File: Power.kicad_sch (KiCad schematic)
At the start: 0 parts

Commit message: Add screw terminal power input and symbol
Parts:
- added C17: 10uF, symbol Device:C
- added C18: 1uF, symbol Device:C
- added C19: 100nF, symbol Device:C
- added J3: 1986660-2, XuLab:CONN2_1986660-2_TEC, symbol XuLab:1986660-2
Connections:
- new net +7.4V: C17.1, C18.1, C19.1, J3.1A, J3.1B
- new net GND: C17.2, C18.2, C19.2, J3.2A, J3.2B

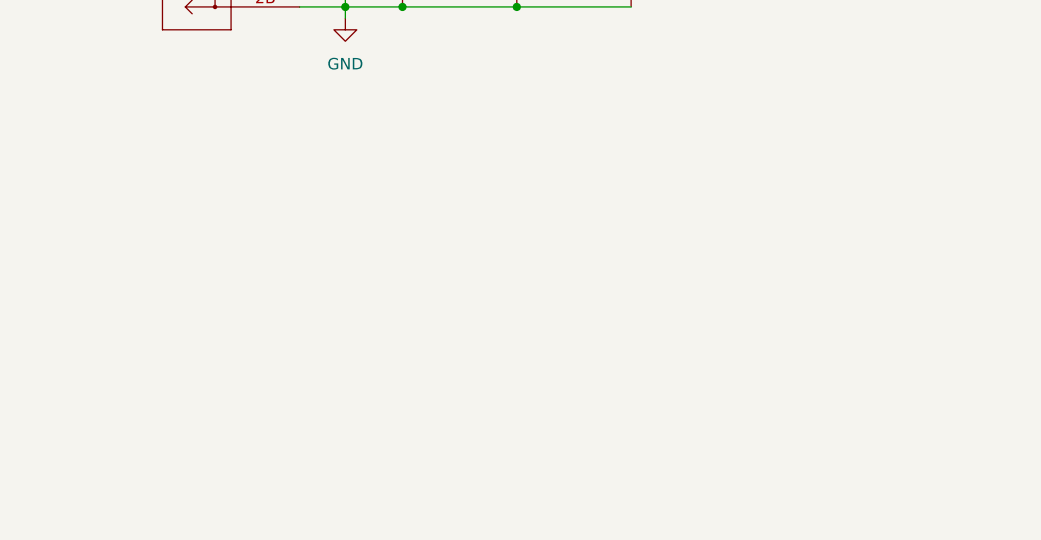
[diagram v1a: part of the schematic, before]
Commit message: Add 3v3 buck converter
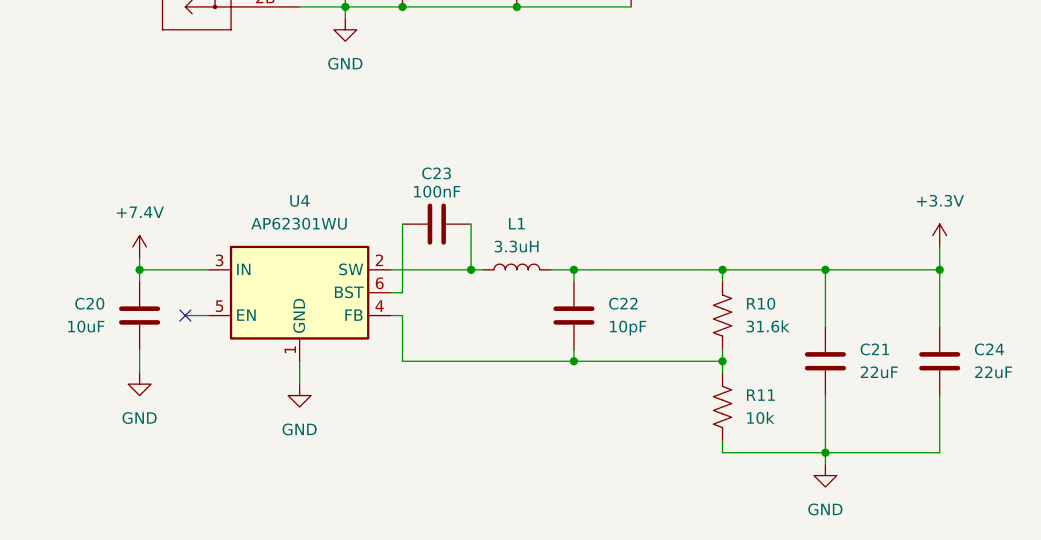
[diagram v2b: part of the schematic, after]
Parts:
- added C20: 10uF, symbol Device:C
- added C21, C24: 22uF, symbol Device:C
- added C22: 10pF, symbol Device:C
- added C23: 100nF, symbol Device:C
- added L1: 3.3uH, symbol Device:L
- added R10: 31.6k, symbol Device:R_US
- added R11: 10k, symbol Device:R_US
- added U4: AP62301WU, Package_TO_SOT_SMD:TSOT-23-6, symbol Regulator_Switching:AP62301WU
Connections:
- net +7.4V: now also C20.1, U4.3 (IN)
- net GND: now also C20.2, C21.2, C24.2, R11.2, U4.1 (GND)
- new net: C22.2, R10.2, R11.1, U4.4 (FB)
- new net: C23.2, L1.1, U4.2 (SW)
- new net: C23.1, U4.6 (BST)
- new net +3.3V: C21.1, C22.1, C24.1, L1.2, R10.1
- no-connect marks 0 -> 1

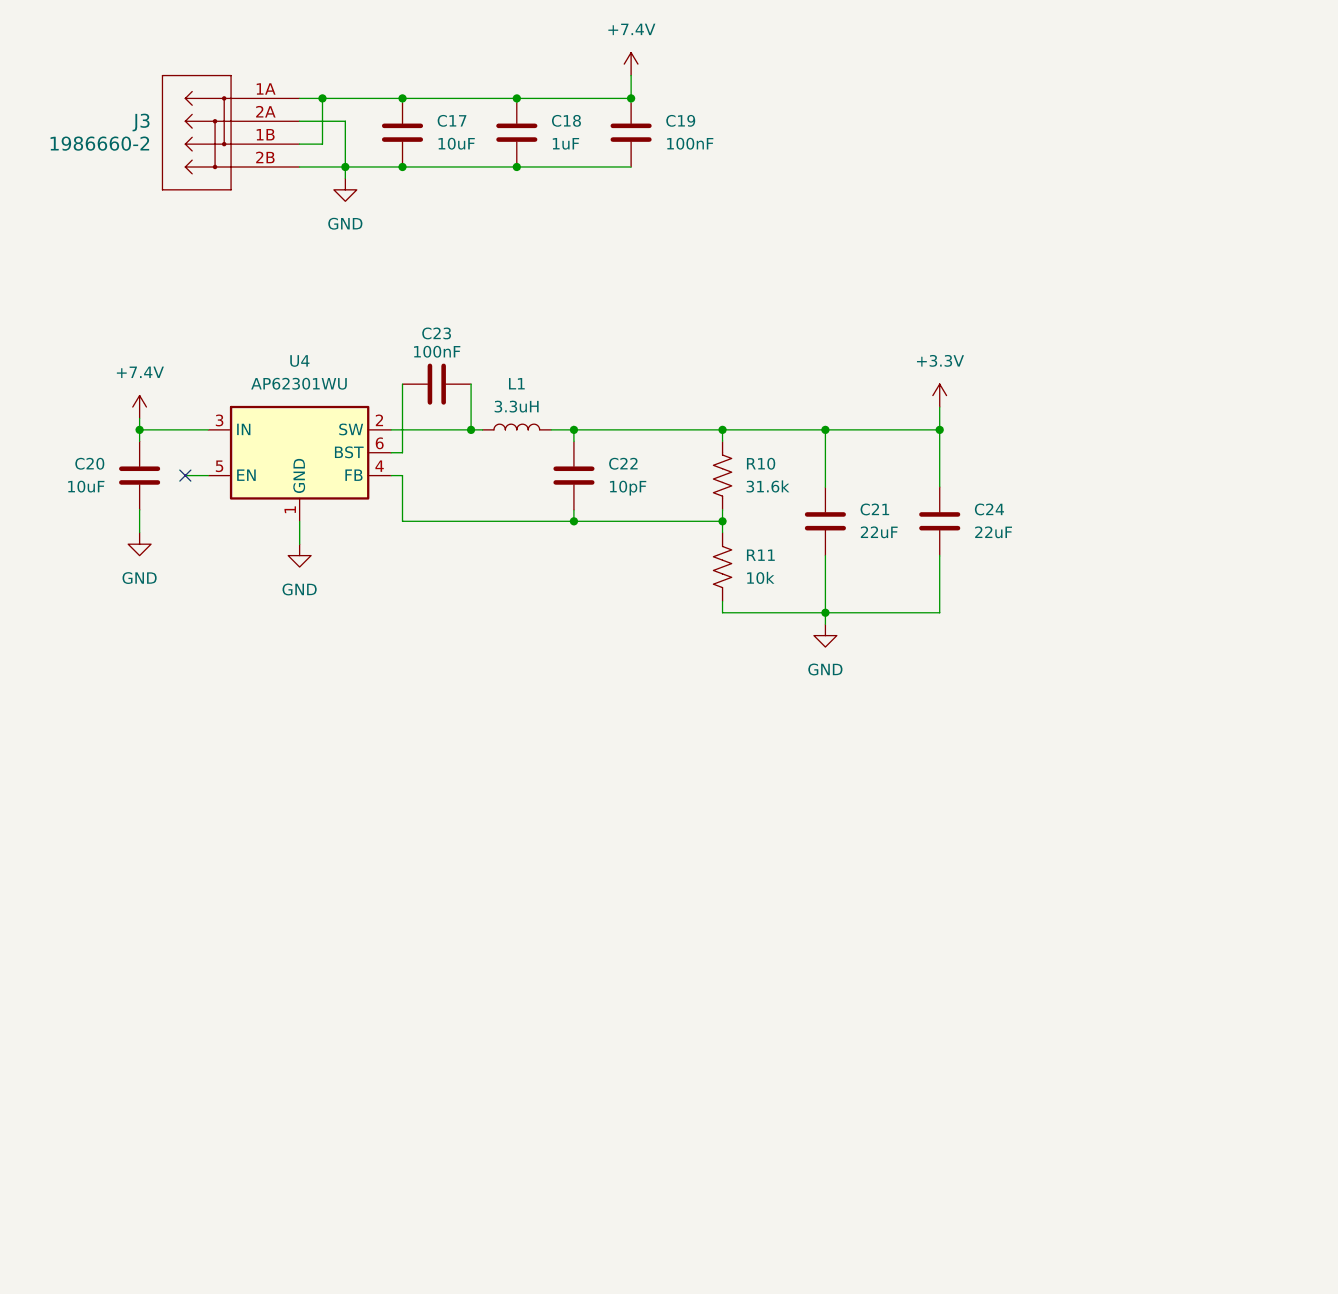
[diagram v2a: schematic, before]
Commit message: Add TVS diodes
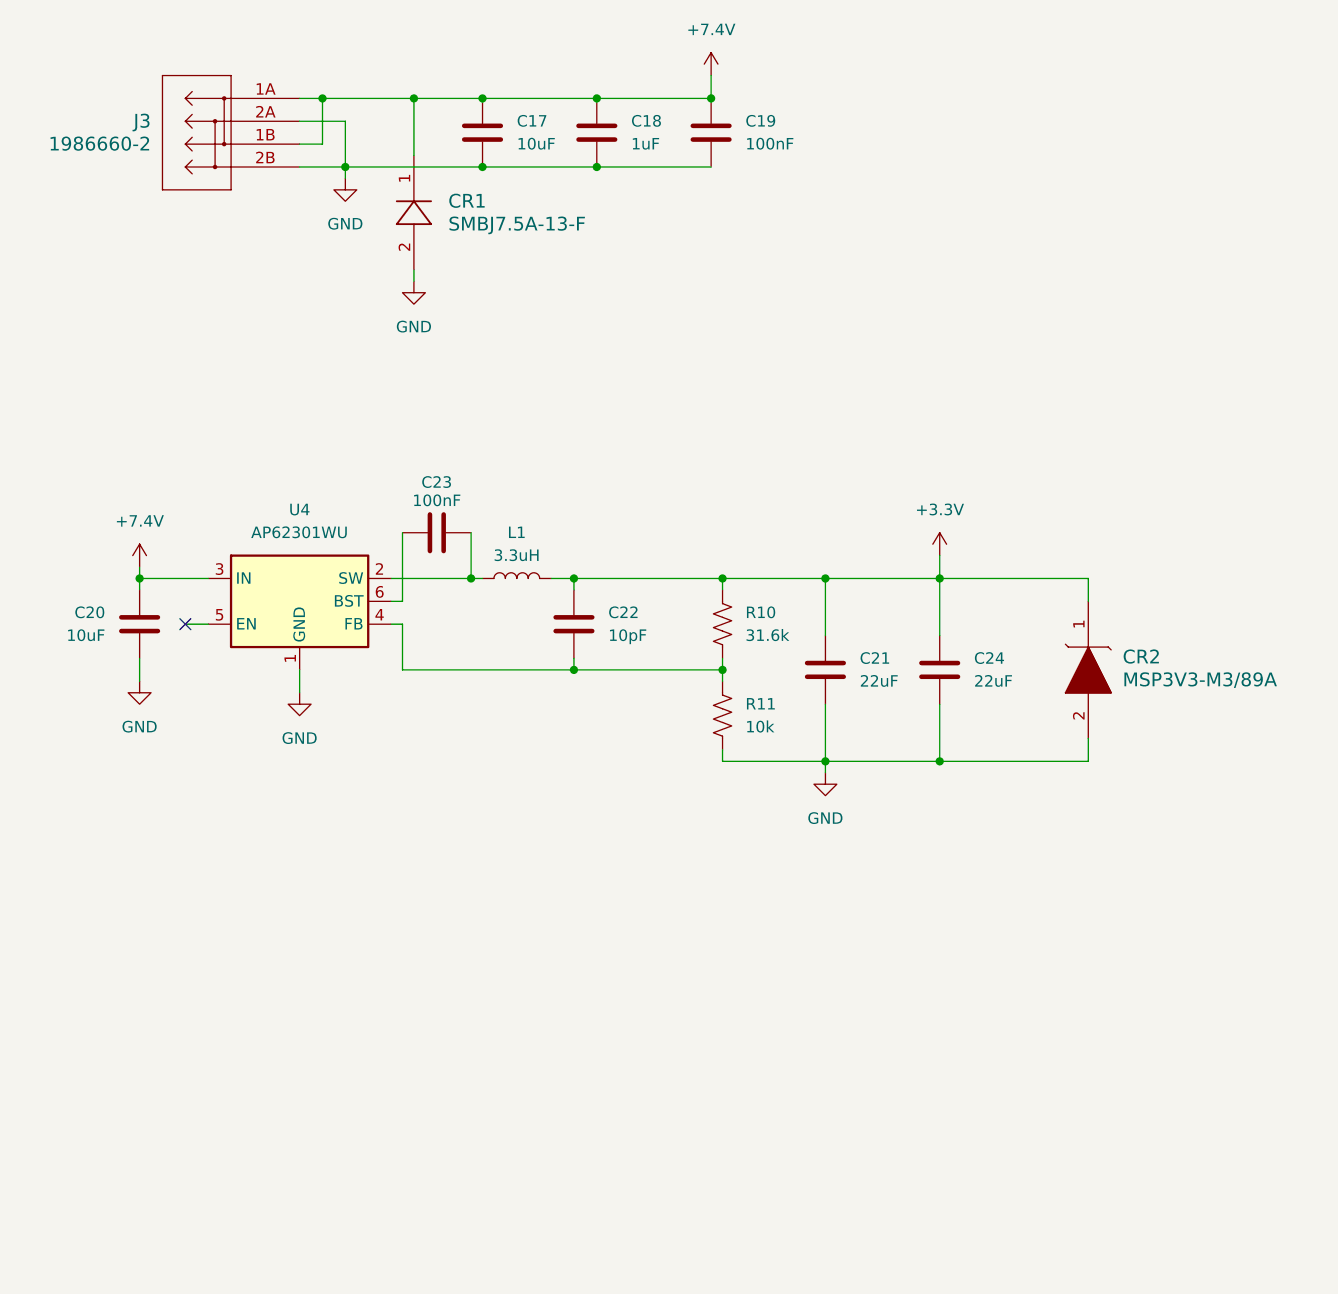
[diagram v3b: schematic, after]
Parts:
- added CR1: SMBJ7.5A-13-F, XuLab:SMB_DIO, symbol XuLab:SMBJ7.5A-13-F
- added CR2: MSP3V3-M3/89A, XuLab:DO-219AD_VIS, symbol XuLab:MSP3V3-M3_89A
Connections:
- net +3.3V: now also CR2.1
- net +7.4V: now also CR1.1
- net GND: now also CR1.2, CR2.2
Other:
- moved on the sheet: C17, C18, C19, C20, C21, C22, C23, C24, L1, R10, R11, U4

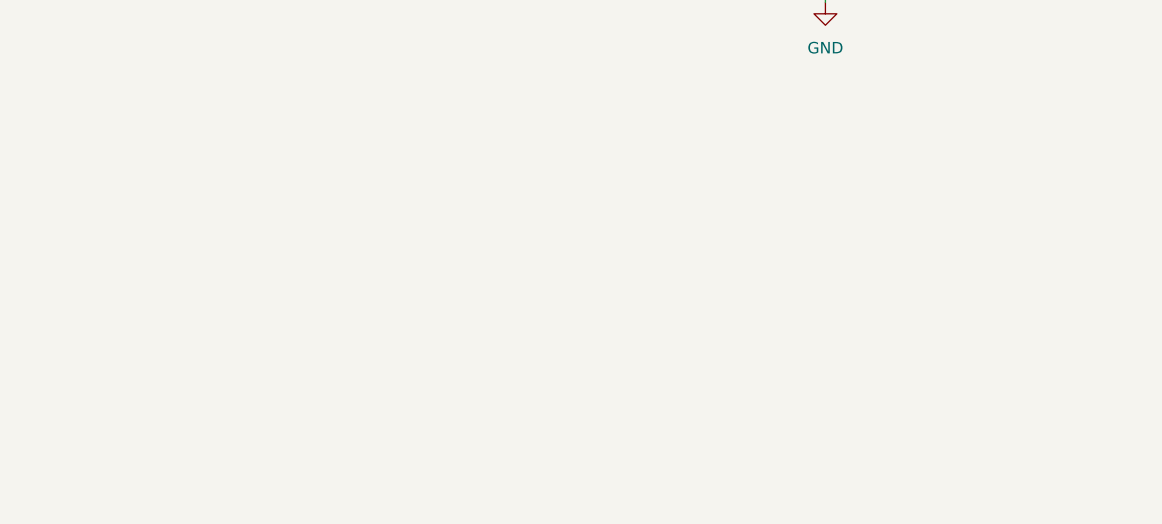
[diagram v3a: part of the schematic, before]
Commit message: Add connectors for servo power
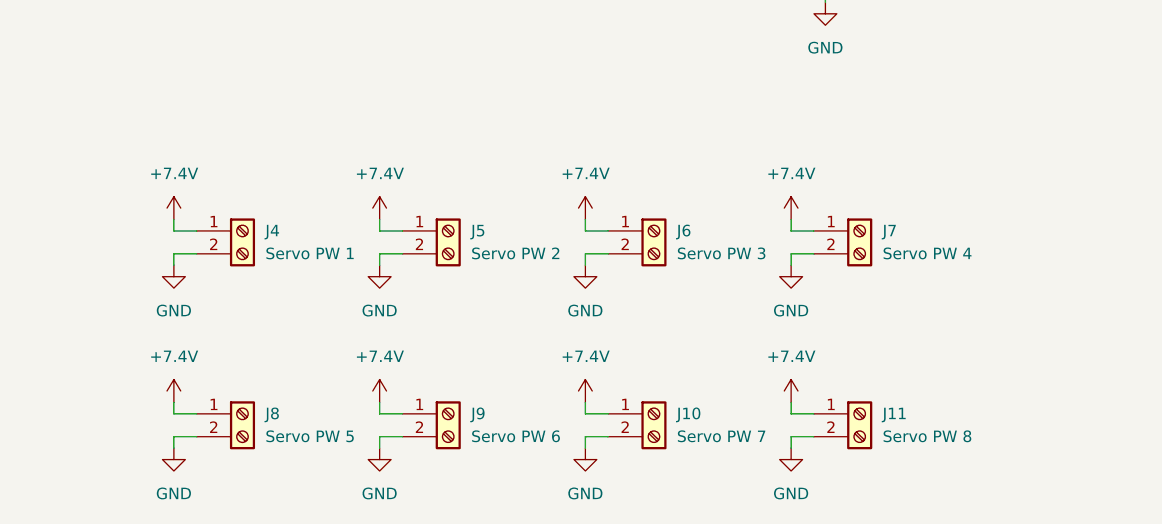
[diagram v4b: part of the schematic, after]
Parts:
- added J10: Servo PW 7, TerminalBlock_Phoenix:TerminalBlock_Phoenix_PT-1,5-2-5.0-H_1x02_P5.00mm_Horizontal, symbol Connector:Screw_Terminal_01x02
- added J11: Servo PW 8, TerminalBlock_Phoenix:TerminalBlock_Phoenix_PT-1,5-2-5.0-H_1x02_P5.00mm_Horizontal, symbol Connector:Screw_Terminal_01x02
- added J4: Servo PW 1, TerminalBlock_Phoenix:TerminalBlock_Phoenix_PT-1,5-2-5.0-H_1x02_P5.00mm_Horizontal, symbol Connector:Screw_Terminal_01x02
- added J5: Servo PW 2, TerminalBlock_Phoenix:TerminalBlock_Phoenix_PT-1,5-2-5.0-H_1x02_P5.00mm_Horizontal, symbol Connector:Screw_Terminal_01x02
- added J6: Servo PW 3, TerminalBlock_Phoenix:TerminalBlock_Phoenix_PT-1,5-2-5.0-H_1x02_P5.00mm_Horizontal, symbol Connector:Screw_Terminal_01x02
- added J7: Servo PW 4, TerminalBlock_Phoenix:TerminalBlock_Phoenix_PT-1,5-2-5.0-H_1x02_P5.00mm_Horizontal, symbol Connector:Screw_Terminal_01x02
- added J8: Servo PW 5, TerminalBlock_Phoenix:TerminalBlock_Phoenix_PT-1,5-2-5.0-H_1x02_P5.00mm_Horizontal, symbol Connector:Screw_Terminal_01x02
- added J9: Servo PW 6, TerminalBlock_Phoenix:TerminalBlock_Phoenix_PT-1,5-2-5.0-H_1x02_P5.00mm_Horizontal, symbol Connector:Screw_Terminal_01x02
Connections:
- net +7.4V: now also J10.1 (Pin_1), J11.1 (Pin_1), J4.1 (Pin_1), J5.1 (Pin_1), J6.1 (Pin_1), J7.1 (Pin_1), J8.1 (Pin_1), J9.1 (Pin_1)
- net GND: now also J10.2 (Pin_2), J11.2 (Pin_2), J4.2 (Pin_2), J5.2 (Pin_2), J6.2 (Pin_2), J7.2 (Pin_2), J8.2 (Pin_2), J9.2 (Pin_2)

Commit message: Add signal outputs for servos and change screw terminal footprints
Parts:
- J10, J11, J4, J5, J6, J7, J8, J9: footprint TerminalBlock_Phoenix:TerminalBlock_Phoenix_PT-1,5-2-5.0-H_1x02_P5.00mm_Horizontal -> TerminalBlock_Phoenix:TerminalBlock_Phoenix_MKDS-1,5-2_1x02_P5.00mm_Horizontal
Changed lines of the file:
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@@
 	(title_block
 		(title "Power")
-		(date "2025-10-24")
+		(date "2025-10-26")
 		(rev "A")
 		(company "CU Boulder Senior Design Team 29 - Xu Lab")
@@
 			)
 		)
-		(property "Footprint" "TerminalBlock_Phoenix:TerminalBlock_Phoenix_PT-1,5-2-5.0-H_1x02_P5.00mm_Horizontal"
+		(property "Footprint" "TerminalBlock_Phoenix:TerminalBlock_Phoenix_MKDS-1,5-2_1x02_P5.00mm_Horizontal"
 			(at 49.53 161.29 0)
 			(effects
@@
 			)
 		)
-		(property "Footprint" "TerminalBlock_Phoenix:TerminalBlock_Phoenix_PT-1,5-2-5.0-H_1x02_P5.00mm_Horizontal"
+		(property "Footprint" "TerminalBlock_Phoenix:TerminalBlock_Phoenix_MKDS-1,5-2_1x02_P5.00mm_Horizontal"
 			(at 118.11 140.97 0)
 			(effects
@@
 			)
 		)
-		(property "Footprint" "TerminalBlock_Phoenix:TerminalBlock_Phoenix_PT-1,5-2-5.0-H_1x02_P5.00mm_Horizontal"
+		(property "Footprint" "TerminalBlock_Phoenix:TerminalBlock_Phoenix_MKDS-1,5-2_1x02_P5.00mm_Horizontal"
 			(at 72.39 140.97 0)
 			(effects
@@
 			)
 		)
-		(property "Footprint" "TerminalBlock_Phoenix:TerminalBlock_Phoenix_PT-1,5-2-5.0-H_1x02_P5.00mm_Horizontal"
+		(property "Footprint" "TerminalBlock_Phoenix:TerminalBlock_Phoenix_MKDS-1,5-2_1x02_P5.00mm_Horizontal"
 			(at 95.25 140.97 0)
 			(effects
@@
 			)
 		)
-		(property "Footprint" "TerminalBlock_Phoenix:TerminalBlock_Phoenix_PT-1,5-2-5.0-H_1x02_P5.00mm_Horizontal"
+		(property "Footprint" "TerminalBlock_Phoenix:TerminalBlock_Phoenix_MKDS-1,5-2_1x02_P5.00mm_Horizontal"
 			(at 49.53 140.97 0)
 			(effects
@@
 			)
 		)
-		(property "Footprint" "TerminalBlock_Phoenix:TerminalBlock_Phoenix_PT-1,5-2-5.0-H_1x02_P5.00mm_Horizontal"
+		(property "Footprint" "TerminalBlock_Phoenix:TerminalBlock_Phoenix_MKDS-1,5-2_1x02_P5.00mm_Horizontal"
 			(at 72.39 161.29 0)
 			(effects
@@
 			)
 		)
-		(property "Footprint" "TerminalBlock_Phoenix:TerminalBlock_Phoenix_PT-1,5-2-5.0-H_1x02_P5.00mm_Horizontal"
+		(property "Footprint" "TerminalBlock_Phoenix:TerminalBlock_Phoenix_MKDS-1,5-2_1x02_P5.00mm_Horizontal"
 			(at 95.25 161.29 0)
 			(effects
@@
 			)
 		)
-		(property "Footprint" "TerminalBlock_Phoenix:TerminalBlock_Phoenix_PT-1,5-2-5.0-H_1x02_P5.00mm_Horizontal"
+		(property "Footprint" "TerminalBlock_Phoenix:TerminalBlock_Phoenix_MKDS-1,5-2_1x02_P5.00mm_Horizontal"
 			(at 118.11 161.29 0)
 			(effects

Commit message: Increase power rail decoupling capacitor values
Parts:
- C17: value 10uF -> 100uF
- C18: value 1uF -> 10uF
- C19: value 100nF -> 1uF
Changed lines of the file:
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@@
 			)
 		)
-		(property "Value" "100nF"
+		(property "Value" "1uF"
 			(at 105.41 45.7199 0)
 			(effects
@@
 			)
 		)
-		(property "Value" "10uF"
+		(property "Value" "100uF"
 			(at 80.01 45.7199 0)
 			(effects
@@
 			)
 		)
-		(property "Value" "1uF"
+		(property "Value" "10uF"
 			(at 92.71 45.7199 0)
 			(effects
